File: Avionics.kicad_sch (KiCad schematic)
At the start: 23 parts, among them SW1 SW_Push, SW2 SW_Push, U3 RP2350B-QFN80

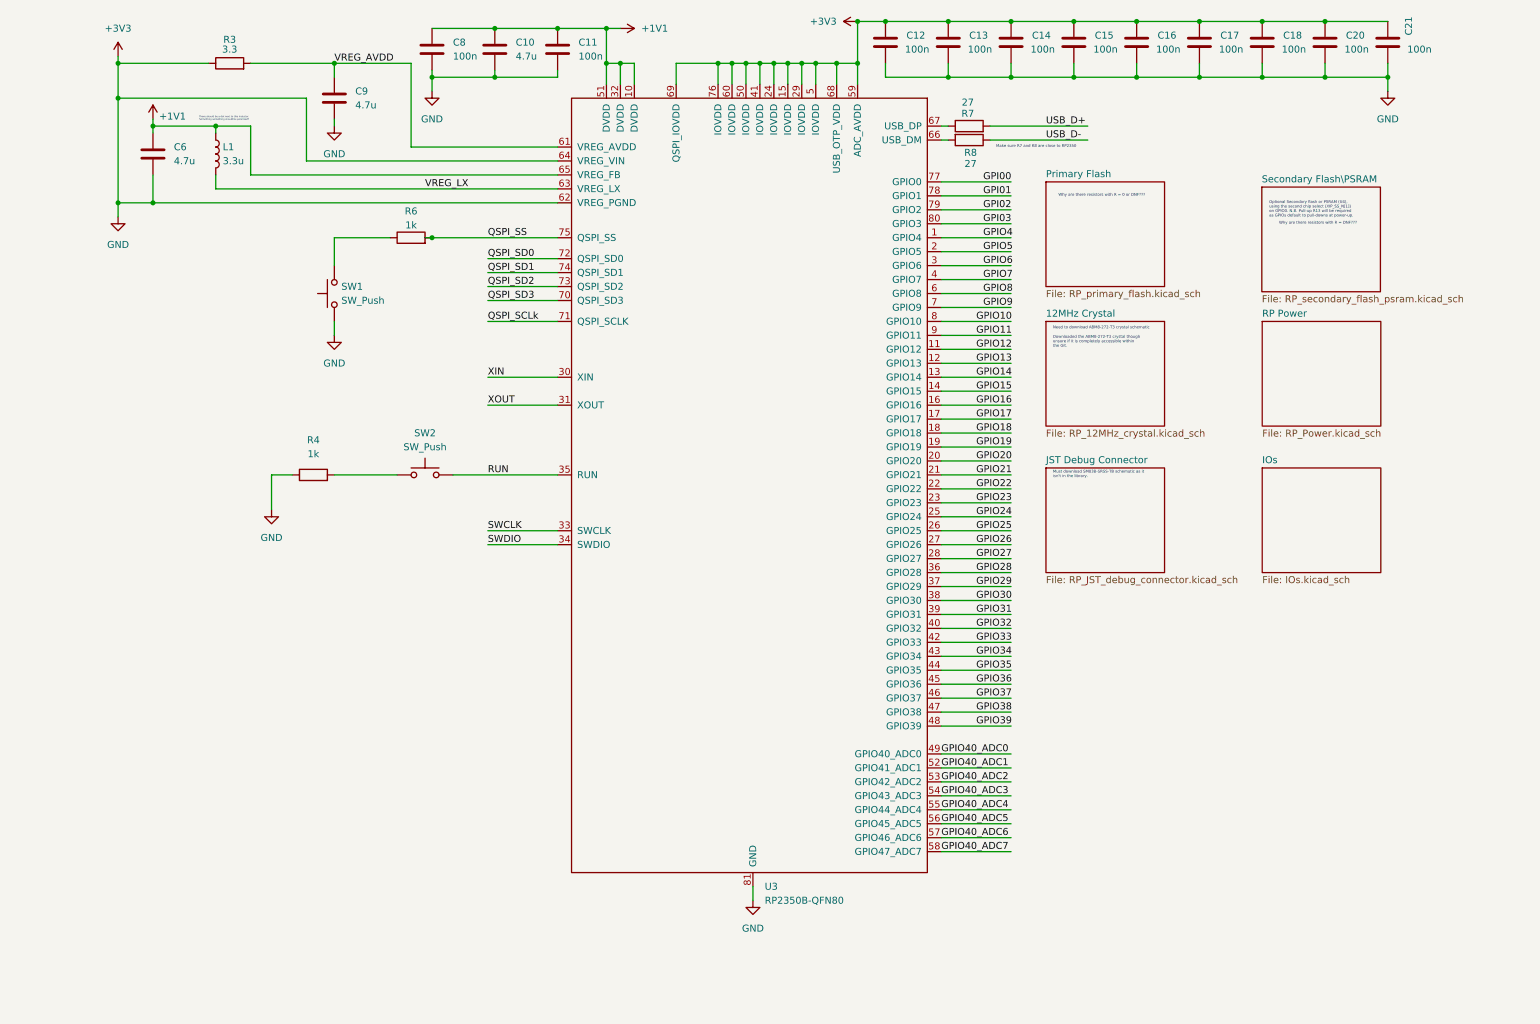
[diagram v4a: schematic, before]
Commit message: Consolidate/mostly finalize avionics
Add RP2350 components to same sheet as RP2350, replace flash with MRAM
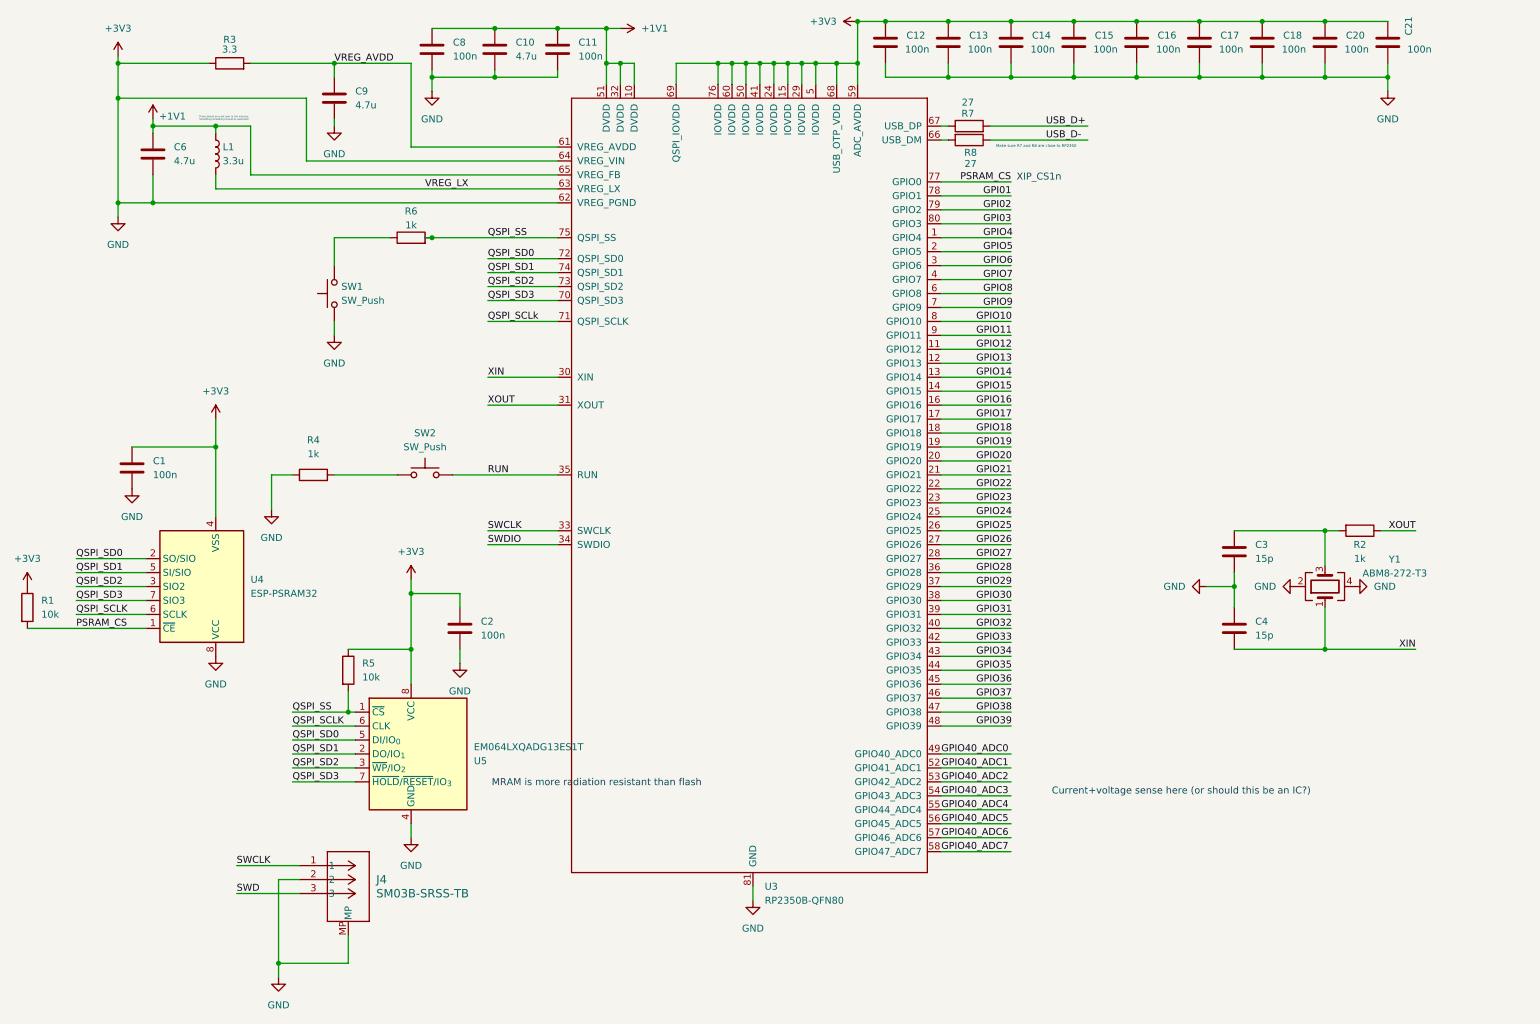
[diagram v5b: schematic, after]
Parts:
- added C1, C2: 100n, symbol Device:C
- added C3, C4: 15p, symbol Device:C
- added J4: SM03B-SRSS-TB, CONN_SM03B-SRSS-TB_JST, symbol 2025-12-23_04-50-52:SM03B-SRSS-TB
- added R1, R5: 10k, symbol Device:R
- added R2: 1k, symbol Device:R
- added U4: ESP-PSRAM32, Package_SO:SOIC-8_3.9x4.9mm_P1.27mm, symbol Memory_RAM:ESP-PSRAM32
- added U5: EM064LXQADG13ES1T, MRAM:WDFN-8-1EP_8x6mm_P1.27mm_EP4.7x4.7, symbol Memory_Flash:W25Q128JVS
- added Y1: ABM8-272-T3, Crystal:Crystal_SMD_3225-4Pin_3.2x2.5mm, symbol Device:Crystal_GND24
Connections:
- net +3V3: now also C1.1, C1.2, C2.1, C2.2, C3.1, C4.2, J4.2, J4.MP, R1.1, R5.1, U4.4 (VSS), U4.8 (VCC), U5.4 (GND), U5.8 (VCC), Y1.2, Y1.4
- net QSPI_SD0: now also U4.2 (SO/SIO), U5.5 (DI/IO_{0})
- net QSPI_SD1: now also U4.5 (SI/SIO), U5.2 (DO/IO_{1})
- net QSPI_SD2: now also U4.3 (SIO2), U5.3 (~{WP}/IO_{2})
- net QSPI_SD3: now also U4.7 (SIO3), U5.7 (~{HOLD}/~{RESET}/IO_{3})
- net QSPI_SS: now also R5.2, U5.1 (~{CS})
- net SWCLK: now also J4.1
- net XIN: now also C4.1, Y1.1
- net XOUT: now also R2.1
- net GPI00 renamed PSRAM_CS
- net PSRAM_CS: now also R1.2, U4.1 (~{CE})
- new net: C3.2, R2.2, Y1.3
- new net QSPI_SCLK: U4.6 (SCLK), U5.6 (CLK)
- new net SWD: J4.3
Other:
- removed sheet 12MHz Crystal
- removed sheet IOs
- removed sheet JST Debug Connector
- removed sheet Primary Flash
- removed sheet RP Power
- removed sheet Secondary Flash\PSRAM
- note added: "Current+voltage sense here (or should this be an IC?)"
- note added: "MRAM is more radiation resistant than flash"
- note added: "XIP_CS1n"
- note removed: "Downloaded the ABM8-272-T3 crystal though unsure if it is completely accessible within the Git."
- note removed: "Must download SM03B-SRSS-TB schematic as it isn't in the library."
- note removed: "Need to download ABM8-272-T3 crystal schematic"
- note removed: "Optional Secondary flash or PSRAM (U4), using the second chip select (XIP_SS_N[1]) on GPIO0. N.B. Pull-up R13 will be required as GPIOs default to pull-downs at power-up."
- note removed: "Why are there resistors with R = 0 or DNF???"
- note removed: "Why are there resistors with R = DNF???"
